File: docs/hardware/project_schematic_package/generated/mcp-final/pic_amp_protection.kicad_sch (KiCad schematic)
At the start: 7 parts, among them J3 LCD, J4 PTT, J5 ENC, J6 TX, J7 SWR, J8 ADC, U1 MCU

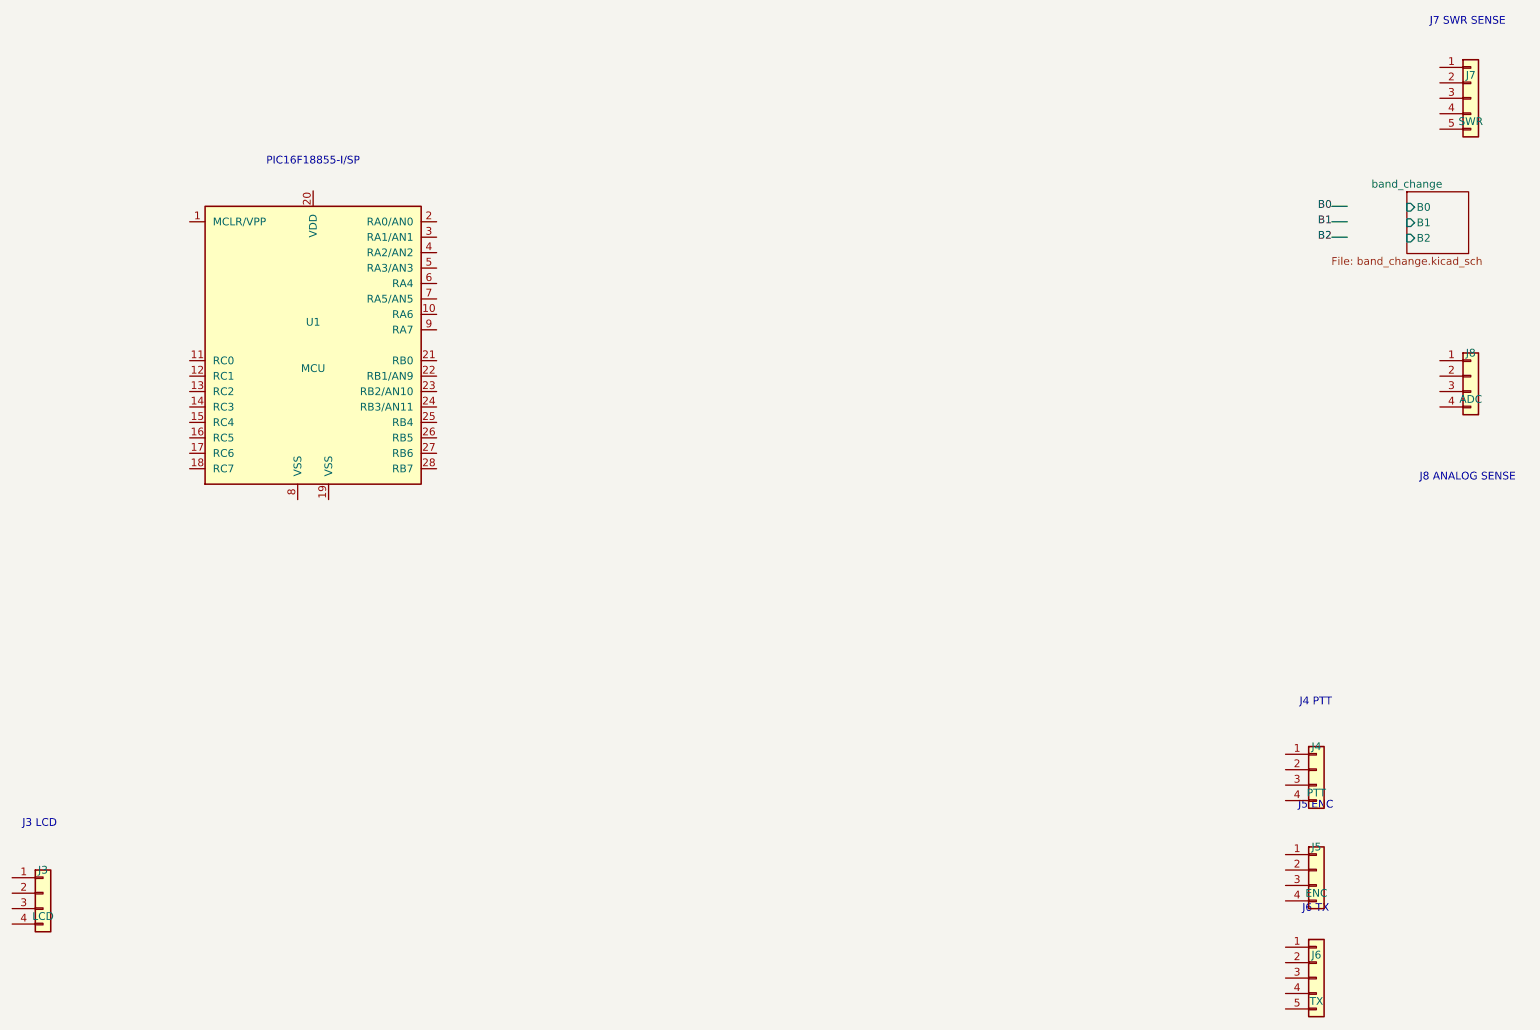
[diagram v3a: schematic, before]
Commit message: Add fan and temperature control block
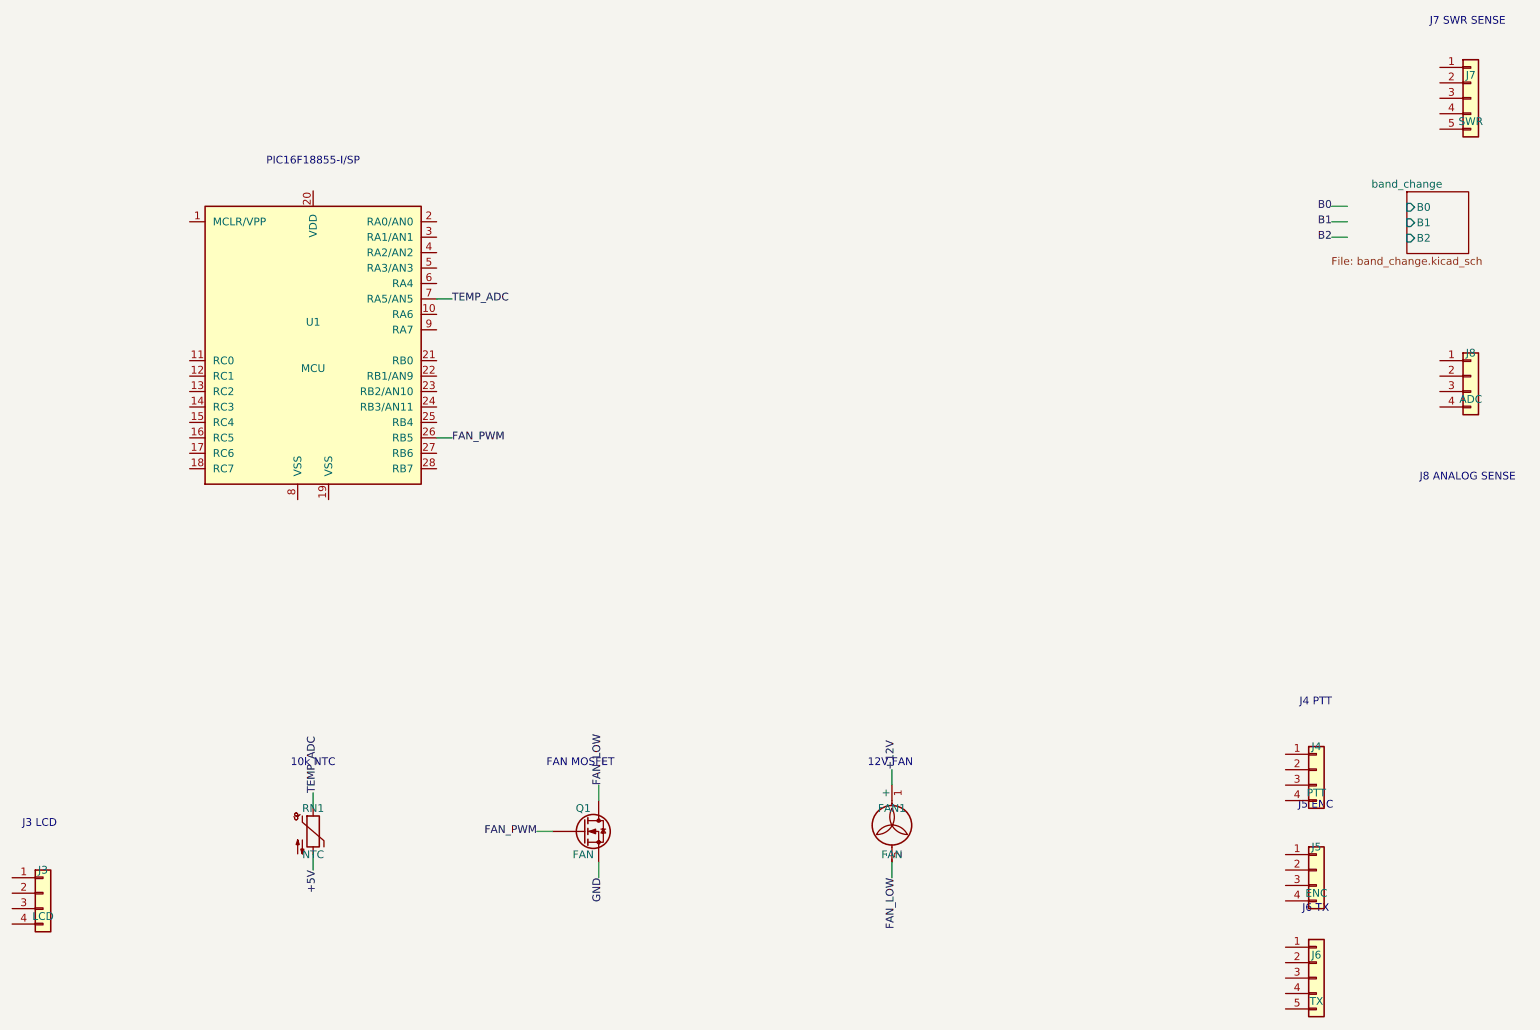
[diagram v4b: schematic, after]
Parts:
- added FAN1: FAN, symbol Motor:Fan
- added Q1: FAN, symbol Device:Q_NMOS
- added RN1: NTC, symbol Device:Thermistor_NTC
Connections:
- net FAN_PWM: now reaches U1.26 (RB5)
- net FAN_PWM: now also Q1.G
- net TEMP_ADC: now reaches U1.7 (RA5/AN5)
- net TEMP_ADC: now also RN1.1
- new net +12V: FAN1.1 (+)
- new net +5V: RN1.2
- new net FAN_LOW: FAN1.2 (-), Q1.D
- new net GND: Q1.S
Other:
- note added: "10k NTC"
- note added: "12V FAN"
- note added: "FAN MOSFET"

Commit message: Direct-wire fan MOSFET and use GND symbol
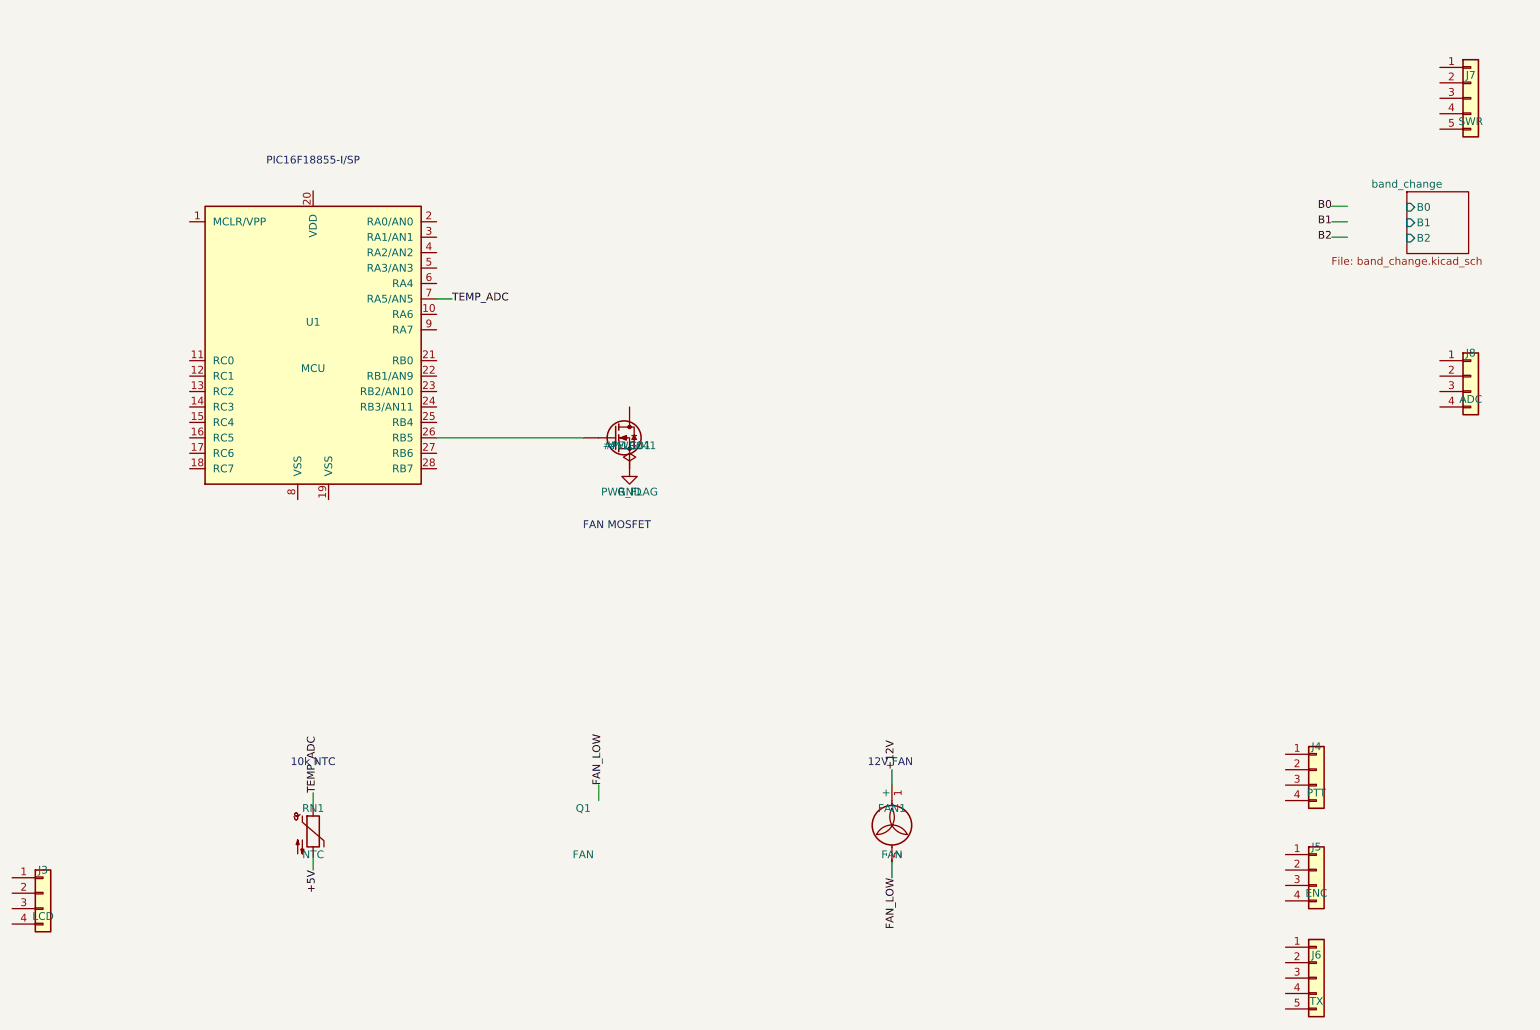
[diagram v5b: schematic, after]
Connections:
- net FAN_LOW: no longer Q1.D
- net FAN_PWM: no longer names the net of Q1.G, U1.26 (RB5)
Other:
- note removed: "J3 LCD"
- note removed: "J4 PTT"
- note removed: "J5 ENC"
- note removed: "J6 TX"
- note removed: "J7 SWR SENSE"
- note removed: "J8 ANALOG SENSE"
- moved on the sheet: Q1
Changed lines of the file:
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@@
 	(lib_name "Device:Q_NMOS")
 	(lib_id "Device:Q_NMOS")
-	(at 124.46 175.26 0)
+	(at 129.54 110.49 0)
 	(unit 1)
 	(exclude_from_sim no)
@@
 	)
 )
+	(symbol
+	(lib_name "power:GND")
+	(lib_id "power:GND")
+	(at 132.08 115.57 0)
+	(unit 1)
+	(exclude_from_sim no)
+	(in_bom yes)
+	(on_board yes)
+	(dnp no)
+	(property "Reference" "#PWR041"
+		(at 132.08 111.76 0)
+		(effects
+			(font
+				(size 1.27 1.27)
+			)
+		)
+	)
+	(property "Value" "GND"
+		(at 132.08 119.38 0)
+		(effects
+			(font
+				(size 1.27 1.27)
+			)
+		)
+	)
+	(property "Footprint" ""
+		(at 132.08 115.57 0)
+		(effects
+			(font
+				(size 1.27 1.27)
+			)
+			(hide yes)
+		)
+	)
+	(property "Datasheet" "~"
+		(at 132.08 115.57 0)
+		(effects
+			(font
+				(size 1.27 1.27)
+			)
+			(hide yes)
+		)
+	)
+	(pin "1"
+)
+	(instances
+		(project "pic_amp_protection"
+			(path "/5f892659-1480-447d-b5a7-bee1c920df64"
+				(reference "#PWR041")
+				(unit 1)
+			)
+		)
+	)
+)
+	(symbol
+	(lib_name "PWR_FLAG")
+	(lib_id "power:PWR_FLAG")
+	(at 132.08 115.57 0)
+	(unit 1)
+	(exclude_from_sim no)
+	(in_bom yes)
+	(on_board yes)
+	(dnp no)
+	(property "Reference" "#FLG01"
+		(at 132.08 111.76 0)
+		(effects
+			(font
+				(size 1.27 1.27)
+			)
+		)
+	)
+	(property "Value" "PWR_FLAG"
+		(at 132.08 119.38 0)
+		(effects
+			(font
+				(size 1.27 1.27)
+			)
+		)
+	)
+	(property "Footprint" ""
+		(at 132.08 115.57 0)
+		(effects
+			(font
+				(size 1.27 1.27)
+			)
+			(hide yes)
+		)
+	)
+	(property "Datasheet" "~"
+		(at 132.08 115.57 0)
+		(effects
+			(font
+				(size 1.27 1.27)
+			)
+			(hide yes)
+		)
+	)
+	(pin "1"
+)
+	(instances
+		(project "pic_amp_protection"
+			(path "/5f892659-1480-447d-b5a7-bee1c920df64"
+				(reference "#FLG01")
+				(unit 1)
+			)
+		)
+	)
+)
 	(symbol_instances
 		(path "/5f892659-1480-447d-b5a7-bee1c920df64/feb0a468-8191-4b22-9d2c-bcba9fc7fc40"
@@
 			(footprint "")
 		)
+		(path "/5f892659-1480-447d-b5a7-bee1c920df64/c068ba2a-ba44-4f70-b69b-ea6285352d5c"
+			(reference "#PWR041")
+			(unit 1)
+			(value "GND")
+			(footprint "")
+		)
+		(path "/5f892659-1480-447d-b5a7-bee1c920df64/e1725c76-5408-4270-a43f-a8c7765c4271"
+			(reference "#FLG01")
+			(unit 1)
+			(value "PWR_FLAG")
+			(footprint "")
+		)
 )
 	(text "PIC16F18855-I/SP"
@@
 	)
 )
-	(text "J3 LCD"
-	(at 35 174 0)
-	(effects
-		(font
-			(size 1.27 1.27)
-		)
-	)
-)
-	(text "J4 PTT"
-	(at 245 154 0)
-	(effects
-		(font
-			(size 1.27 1.27)
-		)
-	)
-)
-	(text "J5 ENC"
-	(at 245 171 0)
-	(effects
-		(font
-			(size 1.27 1.27)
-		)
-	)
-)
-	(text "J6 TX"
-	(at 245 188 0)
-	(effects
-		(font
-			(size 1.27 1.27)
-		)
-	)
-)
-	(text "J7 SWR SENSE"
-	(at 270 42 0)
-	(effects
-		(font
-			(size 1.27 1.27)
-		)
-	)
-)
-	(text "J8 ANALOG SENSE"
-	(at 270 117 0)
-	(effects
-		(font
-			(size 1.27 1.27)
-		)
-	)
-)
-	(text "FAN MOSFET"
-	(at 124 164 0)
-	(effects
-		(font
-			(size 1.27 1.27)
-		)
-	)
-)
 	(text "12V FAN"
 	(at 175 164 0)
@@
 	)
 )
+	(text "FAN MOSFET"
+	(at 130 125 0)
+	(effects
+		(font
+			(size 1.27 1.27)
+		)
+	)
+)
 	(wire
 	(pts
@@
 	(wire
 	(pts
-		(xy 100.33 110.49) (xy 102.87 110.49)
-	)
-	(stroke
-		(width 0)
-		(type default)
-	)
-)
-	(wire
-	(pts
-		(xy 119.38 175.26) (xy 116.84 175.26)
-	)
-	(stroke
-		(width 0)
-		(type default)
-	)
-)
-	(wire
-	(pts
 		(xy 127 170.18) (xy 127 167.64)
 	)
@@
 	(wire
 	(pts
-		(xy 127 180.34) (xy 127 182.88)
-	)
-	(stroke
-		(width 0)
-		(type default)
-	)
-)
-	(wire
-	(pts
 		(xy 100.33 87.63) (xy 102.87 87.63)
 	)
@@
 	(pts
 		(xy 80.01 179.07) (xy 80.01 181.61)
+	)
+	(stroke
+		(width 0)
+		(type default)
+	)
+)
+	(wire
+	(pts
+		(xy 100.33 110.49) (xy 124.46 110.49)
 	)
 	(stroke
@@
 	)
 )
-	(label "FAN_PWM"
-	(at 102.87 110.49 0)
-	(effects
-		(font
-			(size 1.27 1.27)
-		)
-	)
-)
-	(label "FAN_PWM"
-	(at 116.84 175.26 180)
-	(effects
-		(font
-			(size 1.27 1.27)
-		)
-	)
-)
 	(label "FAN_LOW"
 	(at 127 167.64 90)
@@
 	(effects
 		(font
-			(size 1.27 1.27)
-		)
-	)
-)
-	(label "GND"
-	(at 127 182.88 270)
-	(effects
-		(font

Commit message: Initialize fresh MCP schematic project
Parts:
- removed FAN1: FAN, symbol Motor:Fan
- removed J3: LCD, symbol Connector_Generic:Conn_01x04
- removed J4: PTT, symbol Connector_Generic:Conn_01x04
- removed J5: ENC, symbol Connector_Generic:Conn_01x04
- removed J6: TX, symbol Connector_Generic:Conn_01x05
- removed J7: SWR, symbol Connector_Generic:Conn_01x05
- removed J8: ADC, symbol Connector_Generic:Conn_01x04
- removed Q1: FAN, symbol Device:Q_NMOS
- removed RN1: NTC, symbol Device:Thermistor_NTC
- removed U1: MCU, Package_DIP:DIP-28_W7.62mm, symbol PicAmpControl_Symbols:PIC16F18855_I_SP_COMPACT
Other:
- removed sheet band_change
- note removed: "10k NTC"
- note removed: "12V FAN"
- note removed: "FAN MOSFET"
- note removed: "PIC16F18855-I/SP"

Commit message: Checkpoint: MCU + +5V power symbol, verified via direct kicad-cli ERC; add commit-often rule
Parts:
- added U1: PIC16F18855_I_SP_COMPACT, symbol PicAmpControl_Symbols:PIC16F18855_I_SP_COMPACT
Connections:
- new net +5V: U1.20 (VDD)
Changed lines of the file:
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@@
 	(generator "eeschema")
 	(generator_version "9.0")
-	(paper "A4")
+	(paper "A3")
+	(symbol
+	(lib_name "PIC16F18855_I_SP_COMPACT")
+	(lib_id "PicAmpControl_Symbols:PIC16F18855_I_SP_COMPACT")
+	(at 190.5 149.86 0)
+	(unit 1)
+	(exclude_from_sim no)
+	(in_bom yes)
+	(on_board yes)
+	(dnp no)
+	(property "Reference" "U1"
+		(at 190.5 146.05 0)
+		(effects
+			(font
+				(size 1.27 1.27)
+			)
+		)
+	)
+	(property "Value" "PIC16F18855_I_SP_COMPACT"
+		(at 190.5 153.67 0)
+		(effects
+			(font
+				(size 1.27 1.27)
+			)
+		)
+	)
+	(property "Footprint" ""
+		(at 190.5 149.86 0)
+		(effects
+			(font
+				(size 1.27 1.27)
+			)
+			(hide yes)
+		)
+	)
+	(property "Datasheet" "~"
+		(at 190.5 149.86 0)
+		(effects
+			(font
+				(size 1.27 1.27)
+			)
+			(hide yes)
+		)
+	)
+	(pin "1"
+)
+	(pin "10"
+)
+	(pin "11"
+)
+	(pin "12"
+)
+	(pin "13"
+)
+	(pin "14"
+)
+	(pin "15"
+)
+	(pin "16"
+)
+	(pin "17"
+)
+	(pin "18"
+)
+	(pin "19"
+)
+	(pin "2"
+)
+	(pin "20"
+)
+	(pin "21"
+)
+	(pin "22"
+)
+	(pin "23"
+)
+	(pin "24"
+)
+	(pin "25"
+)
+	(pin "26"
+)
+	(pin "27"
+)
+	(pin "28"
+)
+	(pin "3"
+)
+	(pin "4"
+)
+	(pin "5"
+)
+	(pin "6"
+)
+	(pin "7"
+)
+	(pin "8"
+)
+	(pin "9"
+)
+	(instances
+		(project "pic_amp_protection"
+			(path "/8a5f1c10-2087-4dac-b5f6-2b81f7b28d08"
+				(reference "U1")
+				(unit 1)
+			)
+		)
+	)
+)
+	(symbol
+	(lib_name "power:+5V")
+	(lib_id "power:+5V")
+	(at 190.5 124.46 0)
+	(unit 1)
+	(exclude_from_sim no)
+	(in_bom yes)
+	(on_board yes)
+	(dnp no)
+	(property "Reference" "#PWR01"
+		(at 190.5 120.65 0)
+		(effects
+			(font
+				(size 1.27 1.27)
+			)
+		)
+	)
+	(property "Value" "+5V"
+		(at 190.5 128.27 0)
+		(effects
+			(font
+				(size 1.27 1.27)
+			)
+		)
+	)
+	(property "Footprint" ""
+		(at 190.5 124.46 0)
+		(effects
+			(font
+				(size 1.27 1.27)
+			)
+			(hide yes)
+		)
+	)
+	(property "Datasheet" "~"
+		(at 190.5 124.46 0)
+		(effects
+			(font
+				(size 1.27 1.27)
+			)
+			(hide yes)
+		)
+	)
+	(pin "1"
+)
+	(instances
+		(project "pic_amp_protection"
+			(path "/8a5f1c10-2087-4dac-b5f6-2b81f7b28d08"
+				(reference "#PWR01")
+				(unit 1)
+			)
+		)
+	)
+)
+	(symbol
+	(lib_name "PWR_FLAG")
+	(lib_id "power:PWR_FLAG")
+	(at 190.5 124.46 0)
+	(unit 1)
+	(exclude_from_sim no)
+	(in_bom yes)
+	(on_board yes)
+	(dnp no)
+	(property "Reference" "#FLG01"
+		(at 190.5 120.65 0)
+		(effects
+			(font
+				(size 1.27 1.27)
+			)
+		)
+	)
+	(property "Value" "PWR_FLAG"
+		(at 190.5 128.27 0)
+		(effects
+			(font
+				(size 1.27 1.27)
+			)
+		)
+	)
+	(property "Footprint" ""
+		(at 190.5 124.46 0)
+		(effects
+			(font
+				(size 1.27 1.27)
+			)
+			(hide yes)
+		)
+	)
+	(property "Datasheet" "~"
+		(at 190.5 124.46 0)
+		(effects
+			(font
+				(size 1.27 1.27)
+			)
+			(hide yes)
+		)
+	)
+	(pin "1"
+)
+	(instances
+		(project "pic_amp_protection"
+			(path "/8a5f1c10-2087-4dac-b5f6-2b81f7b28d08"
+				(reference "#FLG01")
+				(unit 1)
+			)
+		)
+	)
+)
+	(symbol_instances
+		(path "/8a5f1c10-2087-4dac-b5f6-2b81f7b28d08/e1bbe5ad-06fc-4f47-a4cb-114d0ffd9878"
+			(reference "U1")
+			(unit 1)
+			(value "PIC16F18855_I_SP_COMPACT")
+			(footprint "")
+		)
+		(path "/8a5f1c10-2087-4dac-b5f6-2b81f7b28d08/4262c515-7db0-4f74-8edd-359b845e504e"
+			(reference "#PWR01")
+			(unit 1)
+			(value "+5V")
+			(footprint "")
+		)
+		(path "/8a5f1c10-2087-4dac-b5f6-2b81f7b28d08/897bf177-bda4-43de-9bb7-d52f3ebba95c"
+			(reference "#FLG01")
+			(unit 1)
+			(value "PWR_FLAG")
+			(footprint "")
+		)
+)
 	(sheet_instances
 		(path "/"
